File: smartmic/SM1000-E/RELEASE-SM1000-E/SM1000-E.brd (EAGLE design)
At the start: 65 x 100 mm, 207 parts, among them CN1 HDR100-3, CN10 ST-3509, CN11 HDR100-3, CN12 HRS-A3C-16DA, CN2 JS-MU3-002, CN3 DS-0518, CN4 RJ-45, CN5 ST-3509, CN6 ST-3509, CN7 ST-3509, CN8 ST-3509, CN9 ST-3509, J1 JMP-2PIN, J2 JMP-2PIN, J3 JMP-2PIN, J4 CONN-BOOM-XH-2A, P1 TPAD50, P10 TPAD50, P11 TPAD50, P12 TPAD50, P13 TPAD50, P14 TPAD50, P16 TPAD50, P18 TPAD50, P19 TPAD50, P2 TPAD50, P20 TPAD50, P3 TPAD50, P4 TPAD50, P5 TPAD50, P6 TPAD50, P7 TPAD50, P8 TPAD50, P9 TPAD50, SW1 SW-LC2259, SW2 TS-026, SW3 SW-LC2259EENP, SW4 TS-026, SW5 TS-02B, T1 SM-LP-5001, T2 SM-LP-5001, U1 STM32F405VGT6, U2 LD3985M33R, U3 STMPS2141, U4 EMIF02-USB03F2, U5 TPS54329E, U6 LMV341, U7 LMV341, U8 LM386M-1, U9 LMV341

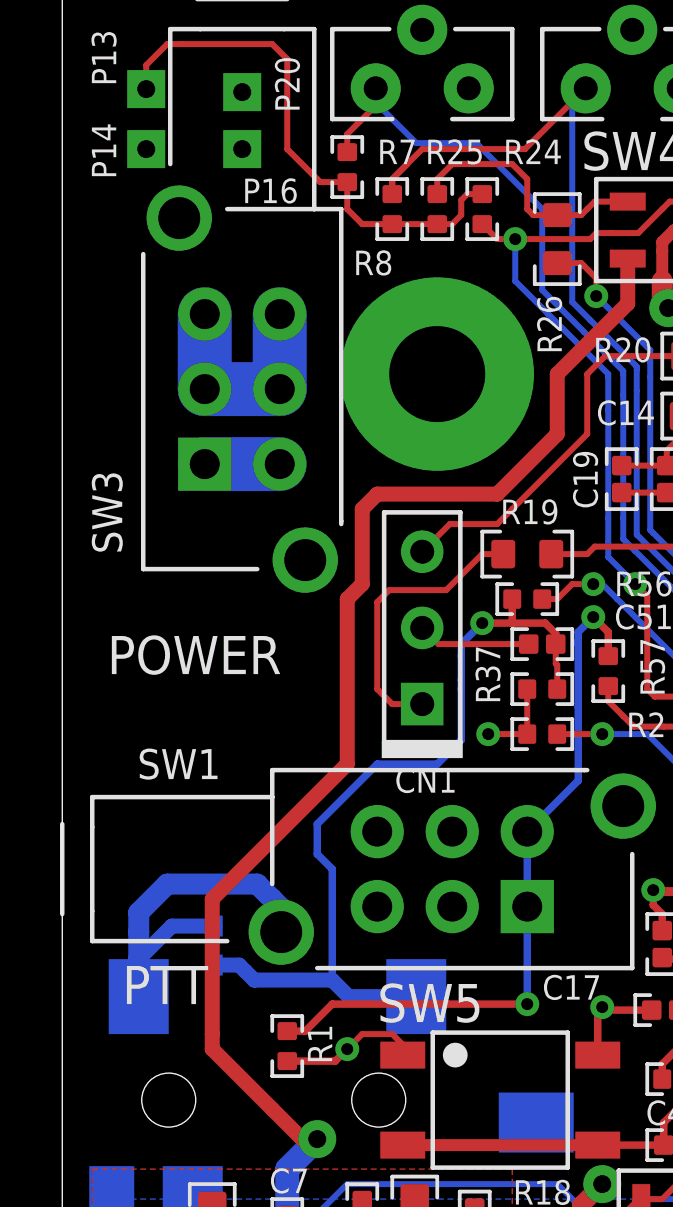
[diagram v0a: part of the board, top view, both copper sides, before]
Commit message: Update pad & drill size on pin 7 of SW1 & SW3.  RGB
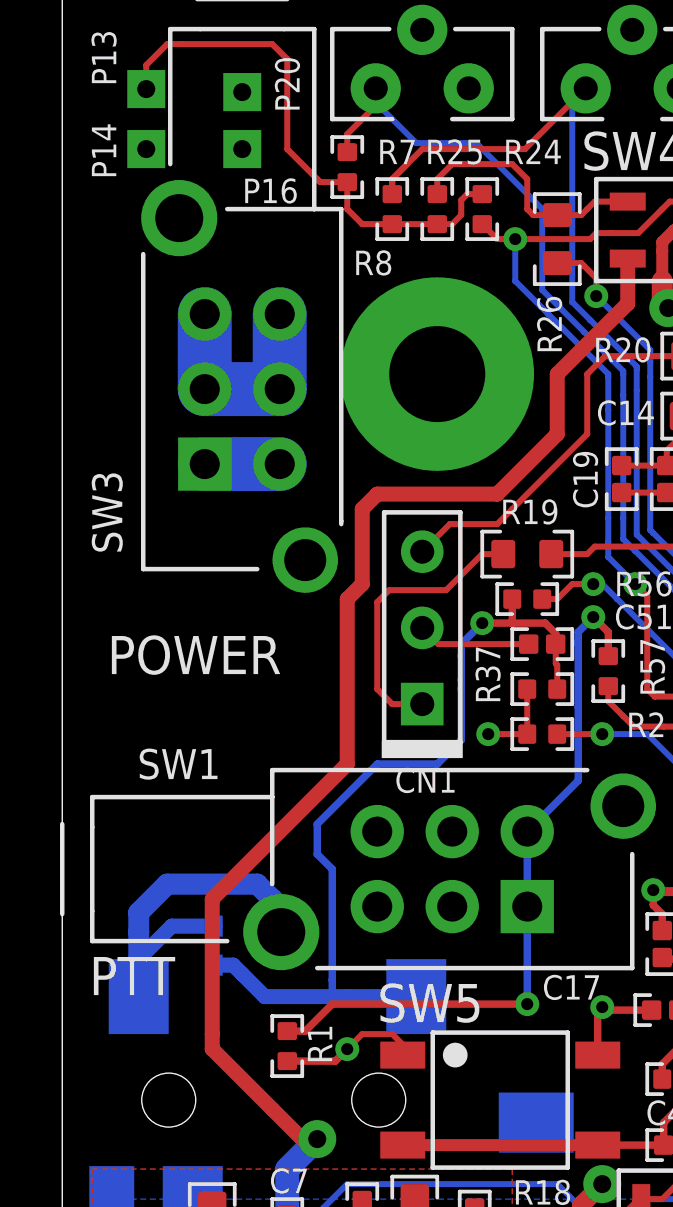
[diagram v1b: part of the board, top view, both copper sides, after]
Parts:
- moved DRILEGEND 0.50 mm to (21.3, -12.2)
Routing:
- net N$15: track 28.5 -> 29.1 mm
